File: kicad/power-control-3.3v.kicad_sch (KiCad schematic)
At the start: 16 parts, among them J5 USB_C_Receptacle_USB2.0, U1 MCP73871, U10 MCP1700x-180xxTT, U11 USBLC6-2P6

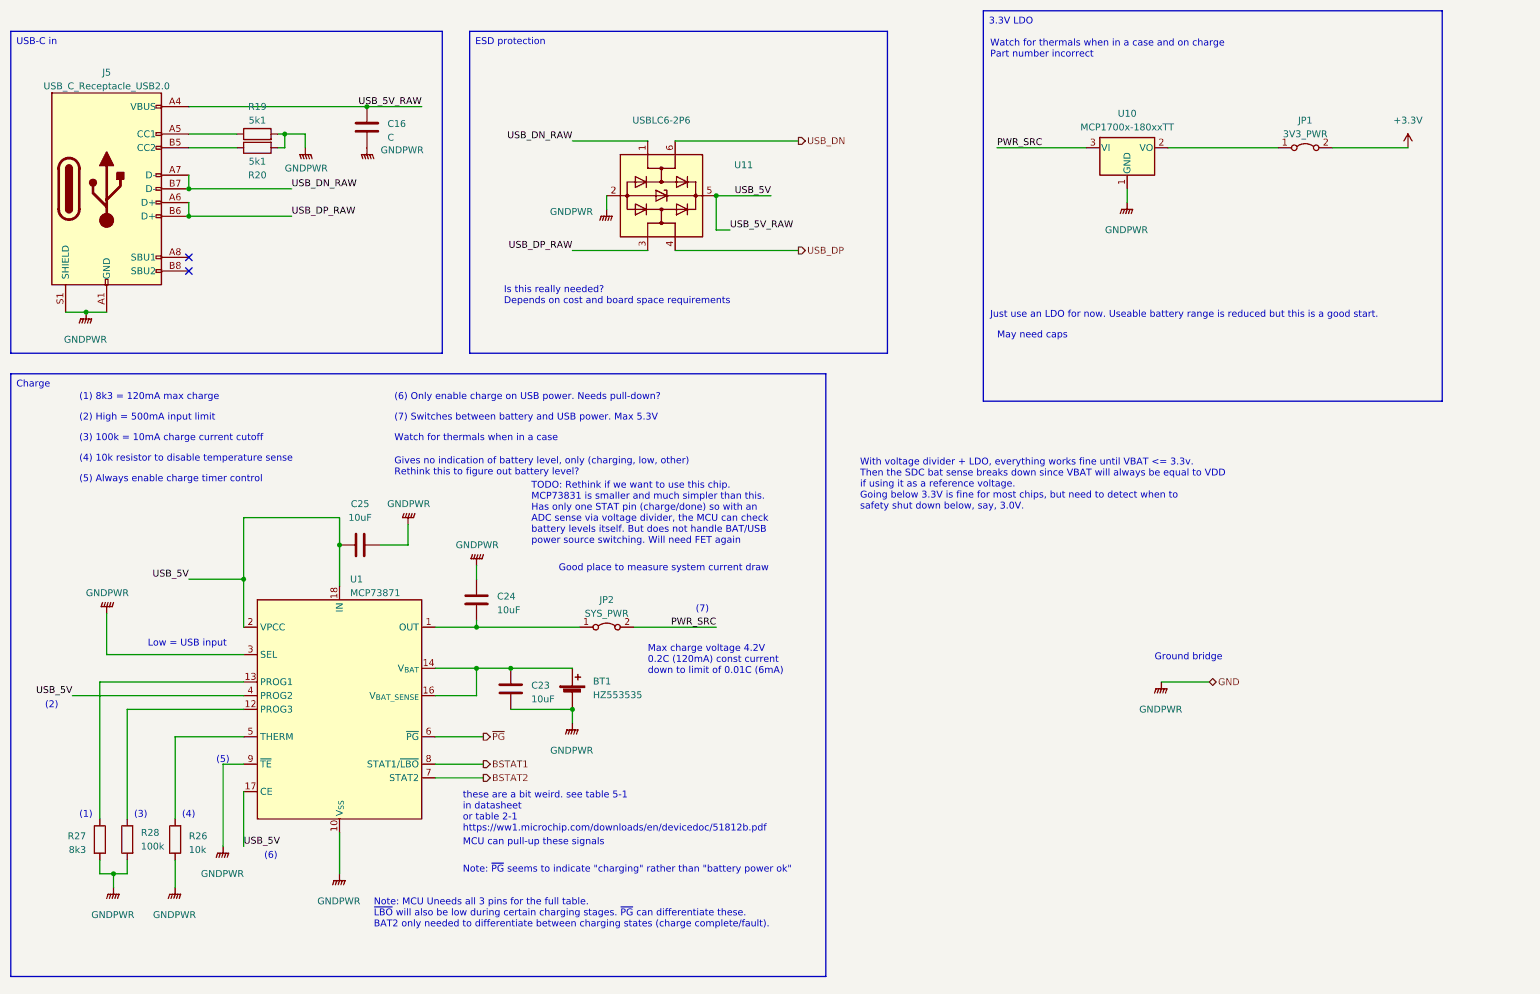
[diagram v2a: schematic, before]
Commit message: hw: change battery to a "simpler" version
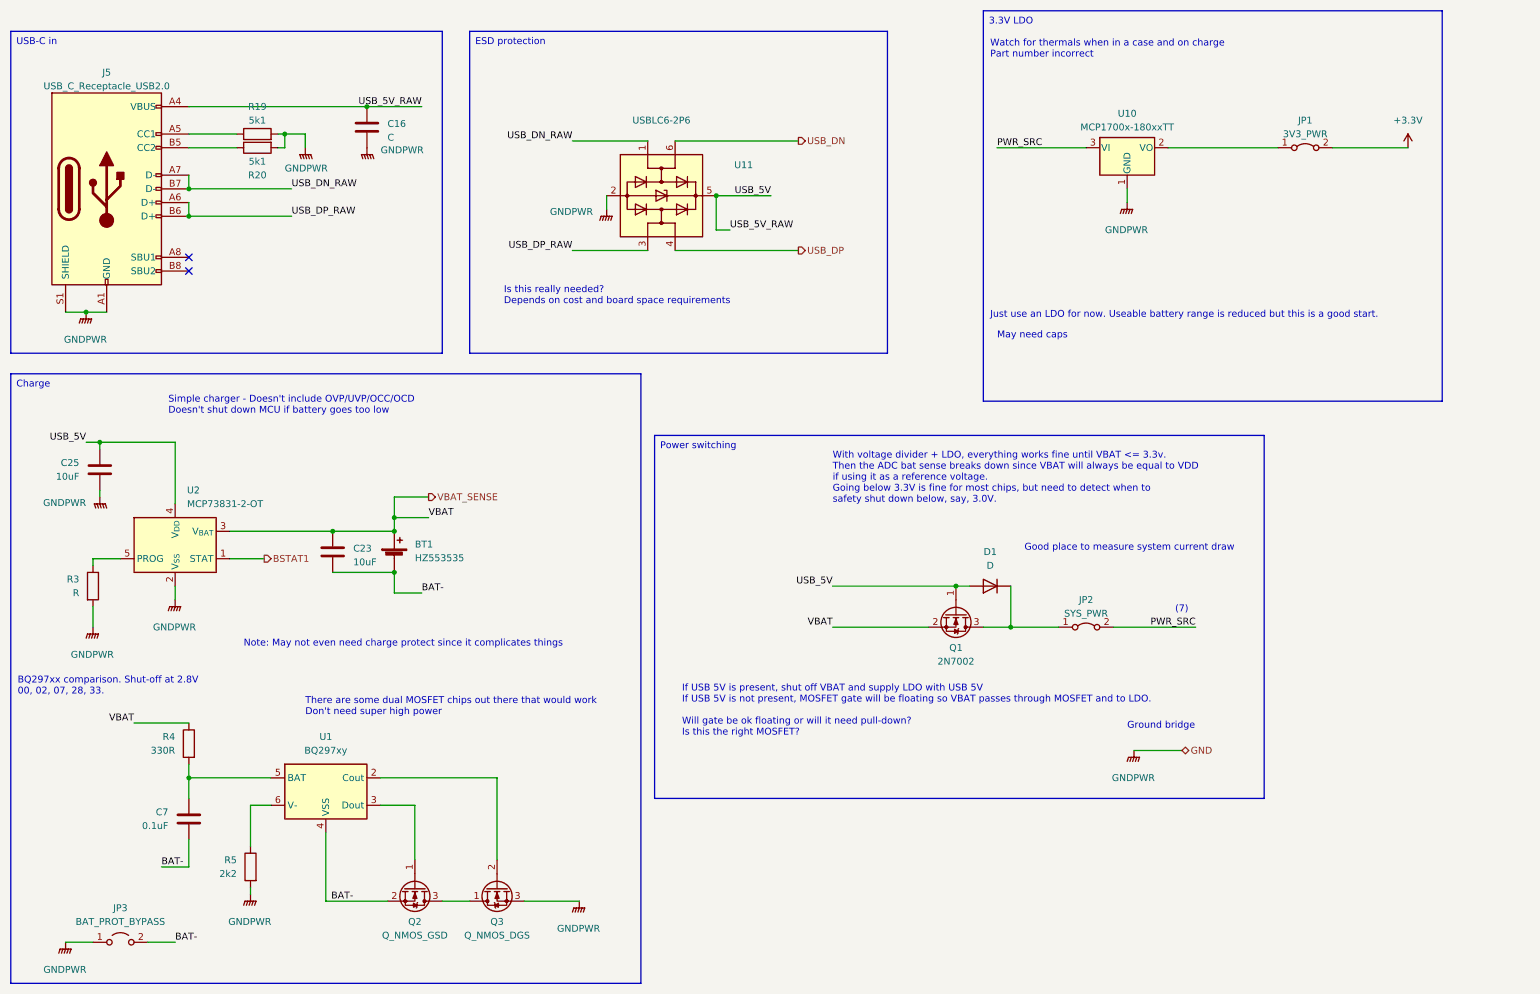
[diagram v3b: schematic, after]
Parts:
- removed C24: 10uF, Capacitor_SMD:C_0402_1005Metric, symbol Device:C
- removed R26: 10k, Capacitor_SMD:C_0402_1005Metric, symbol Device:R
- removed R27: 8k3, Capacitor_SMD:C_0402_1005Metric, symbol Device:R
- removed R28: 100k, Capacitor_SMD:C_0402_1005Metric, symbol Device:R
- removed U1: MCP73871, Package_DFN_QFN:QFN-20-1EP_4x4mm_P0.5mm_EP2.5x2.5mm, symbol Battery_Management:MCP73871
- added C7: 0.1uF, symbol Device:C
- added D1: D, symbol Device:D
- added JP3: BAT_PROT_BYPASS, symbol Jumper:Jumper_2_Open
- added Q1: 2N7002, Package_TO_SOT_SMD:SOT-23, symbol Transistor_FET:2N7002
- added Q2: Q_NMOS_GSD, symbol Device:Q_NMOS_GSD
- added Q3: Q_NMOS_DGS, symbol Device:Q_NMOS_DGS
- added R3: R, symbol Device:R
- added R4: 330R, symbol Device:R
- added R5: 2k2, symbol Device:R
- added U1: BQ297xy, Package_SON:WSON-6_1.5x1.5mm_P0.5mm, symbol Battery_Management:BQ297xy
- added U2: MCP73831-2-OT, Package_TO_SOT_SMD:SOT-23-5, symbol Battery_Management:MCP73831-2-OT
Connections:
- net BSTAT1: now also U2.1 (STAT)
- net GNDPWR: now also C25.1, JP3.1 (A), Q3.3 (S), R3.2, R5.2, U2.2 (V_{SS}); no longer BT1.2 (-), C23.2, C25.2
- net USB_5V: now also C25.2, D1.2 (A), Q1.1 (G), U2.4 (V_{DD}); no longer C25.1
- net at JP2.1 (A): now also D1.1 (K), Q1.3 (D)
- net VBAT_SENSE: now reaches BT1.1 (+), C23.1
- net VBAT_SENSE: now also Q1.2 (S), R4.1, U2.3 (V_{BAT})
- new net: C7.1, R4.2, U1.5 (BAT)
- new net: R5.1, U1.6 (V-)
- new net: R3.1, U2.5 (PROG)
- new net: Q2.3 (D), Q3.1 (D)
- new net: Q3.2 (G), U1.2 (Cout)
- new net: Q2.1 (G), U1.3 (Dout)
- new net BAT-: BT1.2 (-), C23.2, C7.2, JP3.2 (B), Q2.2 (S), U1.4 (VSS)
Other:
- note added: "BQ297xx comparison. Shut-off at 2.8V 00, 02, 07, 28, 33."
- note added: "If USB 5V is present, shut off VBAT and supply LDO with USB 5V If USB 5V is not present, MOSFET gate will be floating so VBAT passes through MOSFET and to LDO. Will gate be ok floating or will it need pull-down? Is this the right MOSFET?"
- note added: "Note: May not even need charge protect since it complicates things"
- note added: "Simple charger - Doesn't include OVP/UVP/OCC/OCD Doesn't shut down MCU if battery goes too low"
- note added: "There are some dual MOSFET chips out there that would work Don't need super high power"
- note added: "With voltage divider + LDO, everything works fine until VBAT <= 3.3v. Then the ADC bat sense breaks down since VBAT will always be equal to VDD if using it as a reference voltage. Going below 3.3V is fine for most chips, but need to detect when to safety shut down below, say, 3.0V."
- note removed: "(1)"
- note removed: "(1) 8k3 = 120mA max charge"
- note removed: "(2)"
- note removed: "(2) High = 500mA input limit"
- note removed: "(3)"
- note removed: "(3) 100k = 10mA charge current cutoff"
- note removed: "(4)"
- note removed: "(4) 10k resistor to disable temperature sense"
- note removed: "(5)"
- note removed: "(5) Always enable charge timer control"
- note removed: "(6)"
- note removed: "(6) Only enable charge on USB power. Needs pull-down?"
- note removed: "(7) Switches between battery and USB power. Max 5.3V"
- note removed: "Gives no indication of battery level, only (charging, low, other) Rethink this to figure out battery level?"
- note removed: "Low = USB input"
- note removed: "MCU can pull-up these signals"
- note removed: "Max charge voltage 4.2V 0.2C (120mA) const current down to limit of 0.01C (6mA)"
- note removed: "Note: MCU Uneeds all 3 pins for the full table. ~{LBO} will also be low during certain charging stages. ~{PG} can differentiate these. BAT2 only needed to differentiate between charging states (charge complete/fault)."
- note removed: "Note: ~{PG} seems to indicate "charging" rather than "battery power ok""
- note removed: "TODO: Rethink if we want to use this chip. MCP73831 is smaller and much simpler than this. Has only one STAT pin (charge/done) so with an ADC sense via voltage divider, the MCU can check battery levels itself. But does not handle BAT/USB power source switching. Will need FET again"
- note removed: "Watch for thermals when in a case"
- note removed: "With voltage divider + LDO, everything works fine until VBAT <= 3.3v. Then the SDC bat sense breaks down since VBAT will always be equal to VDD if using it as a reference voltage. Going below 3.3V is fine for most chips, but need to detect when to safety shut down below, say, 3.0V."
- note removed: "these are a bit weird. see table 5-1 in datasheet or table 2-1 https://ww1.microchip.com/downloads/en/devicedoc/51812b.pdf"
- moved on the sheet: BT1, C23, C25, JP2
